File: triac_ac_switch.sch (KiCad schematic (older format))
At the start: 6 parts, among them U3 FODM3053-NF098

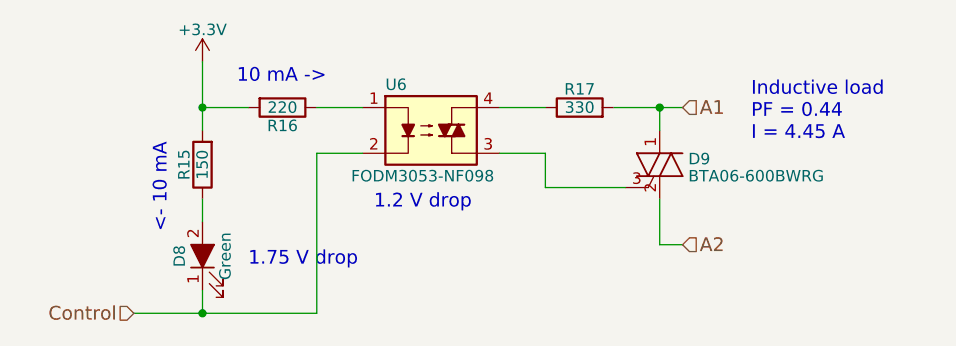
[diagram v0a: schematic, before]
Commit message: 6 output switches, replaced octocoupler
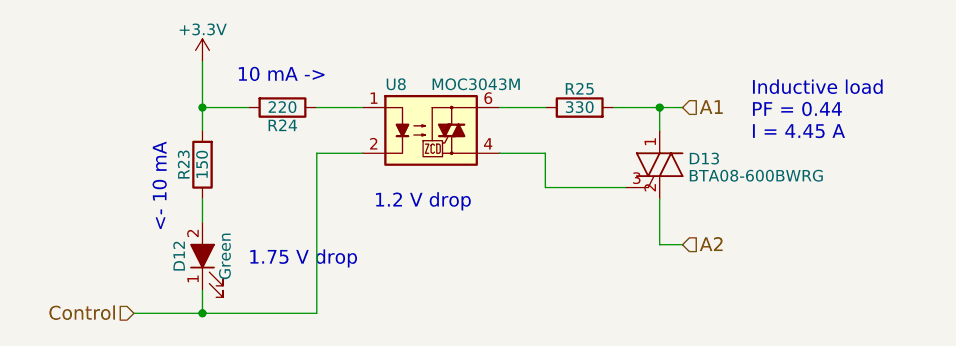
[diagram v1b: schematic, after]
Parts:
- removed U3: FODM3053-NF098, Housings_DIP:DIP-4_W7.62mm_SMD, symbol FODM3052
- added U3: MOC3043M, symbol MOC3043M
- D3: value BTA06-600BWRG -> BTA08-600BWRG
- renumbered R8 to R10, R6 to R8, R7 to R9
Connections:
- net Control: now also U3.2
- net at D3.3 (G): now also U3.4
- net at R9.1: now also U3.1
- net at R10.1: now also U3.6
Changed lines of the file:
@@
 $Descr A4 11693 8268
 encoding utf-8
-Sheet 2 5
+Sheet 2 7
 Title ""
 Date ""
@@
 AR Path="/5ACECAA1/5ACD7198" Ref="D7"  Part="1"
 AR Path="/5ACED0B2/5ACD7198" Ref="D9"  Part="1"
-F 0 "D9" H 4975 5575 50  0000 L CNN
-F 1 "BTA06-600BWRG" H 4975 5500 50  0000 L CNN
+AR Path="/5AD64C62/5ACD7198" Ref="D11"  Part="1"
+AR Path="/5AD65085/5ACD7198" Ref="D13"  Part="1"
+F 0 "D13" H 4975 5575 50  0000 L CNN
+F 1 "BTA08-600BWRG" H 4975 5500 50  0000 L CNN
 F 2 "" V 4925 5575 50  0001 C CNN
 F 3 "" V 4850 5550 50  0001 C CNN
 	1    4850 5550
-	1    0    0    -1
-$EndComp
-$Comp
-L FODM3052 U3
-U 1 1 5ACD7247
-P 3850 5400
-AR Path="/5ACD7149/5ACD7247" Ref="U3"  Part="1"
-AR Path="/5ACE052D/5ACD7247" Ref="U4"  Part="1"
-AR Path="/5ACECAA1/5ACD7247" Ref="U5"  Part="1"
-AR Path="/5ACED0B2/5ACD7247" Ref="U6"  Part="1"
-F 0 "U6" H 3650 5600 50  0000 L CNN
-F 1 "FODM3053-NF098" H 3500 5200 50  0000 L CNN
-F 2 "Housings_DIP:DIP-4_W7.62mm_SMD" H 3650 5200 50  0001 L CIN
-F 3 "" H 3825 5400 50  0001 L CNN
-	1    3850 5400
 	1    0    0    -1
 $EndComp
@@
 AR Path="/5ACECAA1/5ACDBD28" Ref="#PWR034"  Part="1"
 AR Path="/5ACED0B2/5ACDBD28" Ref="#PWR035"  Part="1"
-F 0 "#PWR035" H 2850 4950 50  0001 C CNN
+AR Path="/5AD64C62/5ACDBD28" Ref="#PWR036"  Part="1"
+AR Path="/5AD65085/5ACDBD28" Ref="#PWR037"  Part="1"
+F 0 "#PWR037" H 2850 4950 50  0001 C CNN
 F 1 "+3.3V" H 2850 5240 50  0000 C CNN
 F 2 "" H 2850 5100 50  0001 C CNN
@@
 $EndComp
 $Comp
-L R R7
+L R R9
 U 1 1 5ACDBD40
 P 3200 5300
-AR Path="/5ACD7149/5ACDBD40" Ref="R7"  Part="1"
-AR Path="/5ACE052D/5ACDBD40" Ref="R10"  Part="1"
-AR Path="/5ACECAA1/5ACDBD40" Ref="R13"  Part="1"
-AR Path="/5ACED0B2/5ACDBD40" Ref="R16"  Part="1"
-F 0 "R16" V 3280 5300 50  0000 C CNN
+AR Path="/5ACD7149/5ACDBD40" Ref="R9"  Part="1"
+AR Path="/5ACE052D/5ACDBD40" Ref="R12"  Part="1"
+AR Path="/5ACECAA1/5ACDBD40" Ref="R15"  Part="1"
+AR Path="/5ACED0B2/5ACDBD40" Ref="R18"  Part="1"
+AR Path="/5AD64C62/5ACDBD40" Ref="R21"  Part="1"
+AR Path="/5AD65085/5ACDBD40" Ref="R24"  Part="1"
+F 0 "R24" V 3280 5300 50  0000 C CNN
 F 1 "220" V 3200 5300 50  0000 C CNN
 F 2 "" V 3130 5300 50  0001 C CNN
@@
 AR Path="/5ACECAA1/5ACDC9FE" Ref="D6"  Part="1"
 AR Path="/5ACED0B2/5ACDC9FE" Ref="D8"  Part="1"
-F 0 "D8" H 2850 6050 50  0000 C CNN
+AR Path="/5AD64C62/5ACDC9FE" Ref="D10"  Part="1"
+AR Path="/5AD65085/5ACDC9FE" Ref="D12"  Part="1"
+F 0 "D12" H 2850 6050 50  0000 C CNN
 F 1 "Green" H 2850 5850 50  0000 C CNN
 F 2 "" H 2850 5950 50  0001 C CNN
@@
 10 mA ->
 $Comp
-L R R6
+L R R8
 U 1 1 5ACDCB25
 P 2850 5550
-AR Path="/5ACD7149/5ACDCB25" Ref="R6"  Part="1"
-AR Path="/5ACE052D/5ACDCB25" Ref="R9"  Part="1"
-AR Path="/5ACECAA1/5ACDCB25" Ref="R12"  Part="1"
-AR Path="/5ACED0B2/5ACDCB25" Ref="R15"  Part="1"
-F 0 "R15" V 2930 5550 50  0000 C CNN
+AR Path="/5ACD7149/5ACDCB25" Ref="R8"  Part="1"
+AR Path="/5ACE052D/5ACDCB25" Ref="R11"  Part="1"
+AR Path="/5ACECAA1/5ACDCB25" Ref="R14"  Part="1"
+AR Path="/5ACED0B2/5ACDCB25" Ref="R17"  Part="1"
+AR Path="/5AD64C62/5ACDCB25" Ref="R20"  Part="1"
+AR Path="/5AD65085/5ACDCB25" Ref="R23"  Part="1"
+F 0 "R23" V 2930 5550 50  0000 C CNN
 F 1 "150" V 2850 5550 50  0000 C CNN
 F 2 "" V 2780 5550 50  0001 C CNN
@@
 A1
 $Comp
-L R R8
+L R R10
 U 1 1 5ACDCE47
 P 4500 5300
-AR Path="/5ACD7149/5ACDCE47" Ref="R8"  Part="1"
-AR Path="/5ACE052D/5ACDCE47" Ref="R11"  Part="1"
-AR Path="/5ACECAA1/5ACDCE47" Ref="R14"  Part="1"
-AR Path="/5ACED0B2/5ACDCE47" Ref="R17"  Part="1"
-F 0 "R17" V 4580 5300 50  0000 C CNN
+AR Path="/5ACD7149/5ACDCE47" Ref="R10"  Part="1"
+AR Path="/5ACE052D/5ACDCE47" Ref="R13"  Part="1"
+AR Path="/5ACECAA1/5ACDCE47" Ref="R16"  Part="1"
+AR Path="/5ACED0B2/5ACDCE47" Ref="R19"  Part="1"
+AR Path="/5AD64C62/5ACDCE47" Ref="R22"  Part="1"
+AR Path="/5AD65085/5ACDCE47" Ref="R25"  Part="1"
+F 0 "R25" V 4580 5300 50  0000 C CNN
 F 1 "330" V 4500 5300 50  0000 C CNN
 F 2 "" V 4430 5300 50  0001 C CNN
@@
 Text Notes 5250 5450 0    60   ~ 0
 Inductive load\nPF = 0.44\nI = 4.45 A
+$Comp
+L MOC3043M U3
+U 1 1 5AD5E652
+P 3850 5400
+AR Path="/5ACD7149/5AD5E652" Ref="U3"  Part="1"
+AR Path="/5ACE052D/5AD5E652" Ref="U4"  Part="1"
+AR Path="/5ACECAA1/5AD5E652" Ref="U5"  Part="1"
+AR Path="/5ACED0B2/5AD5E652" Ref="U6"  Part="1"
+AR Path="/5AD64C62/5AD5E652" Ref="U7"  Part="1"
+AR Path="/5AD65085/5AD5E652" Ref="U8"  Part="1"
+F 0 "U8" H 3650 5600 50  0000 L CNN
+F 1 "MOC3043M" H 3850 5600 50  0000 L CNN
+F 2 "" H 3650 5200 50  0001 L CIN
+F 3 "" H 3815 5400 50  0001 L CNN
+	1    3850 5400
+	1    0    0    -1
+$EndComp
 $EndSCHEMATC
